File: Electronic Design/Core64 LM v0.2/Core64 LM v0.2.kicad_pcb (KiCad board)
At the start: 2 copper layers, 85 x 85 mm, 88 parts, among them J1 PASS THROUGH BOARD, J2 PASS THROUGH BOARD, J3 Conn_01x01_Male, J4 Conn_01x01_Male, J5 Conn_01x01_Male, J6 Conn_01x01_Male

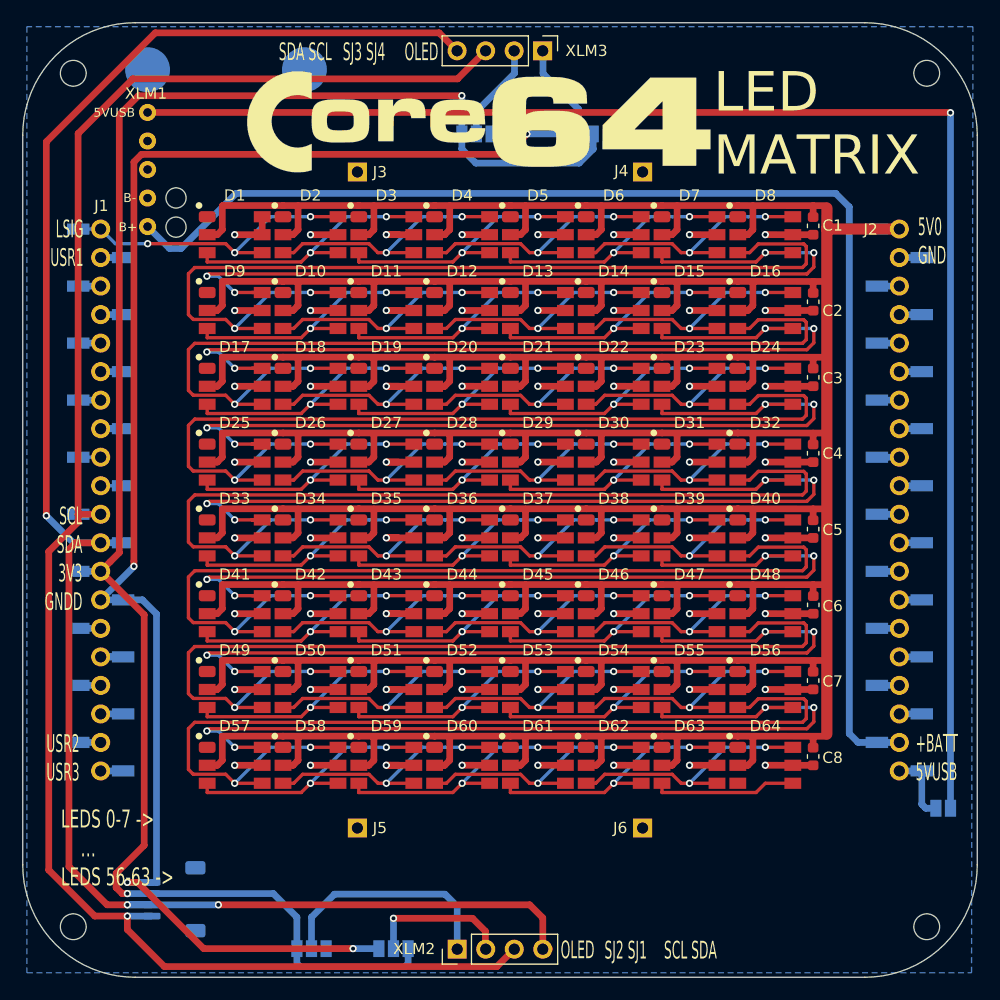
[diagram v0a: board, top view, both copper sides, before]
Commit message: Refine layout placement of QWIIC and silkscreen, add battery markers
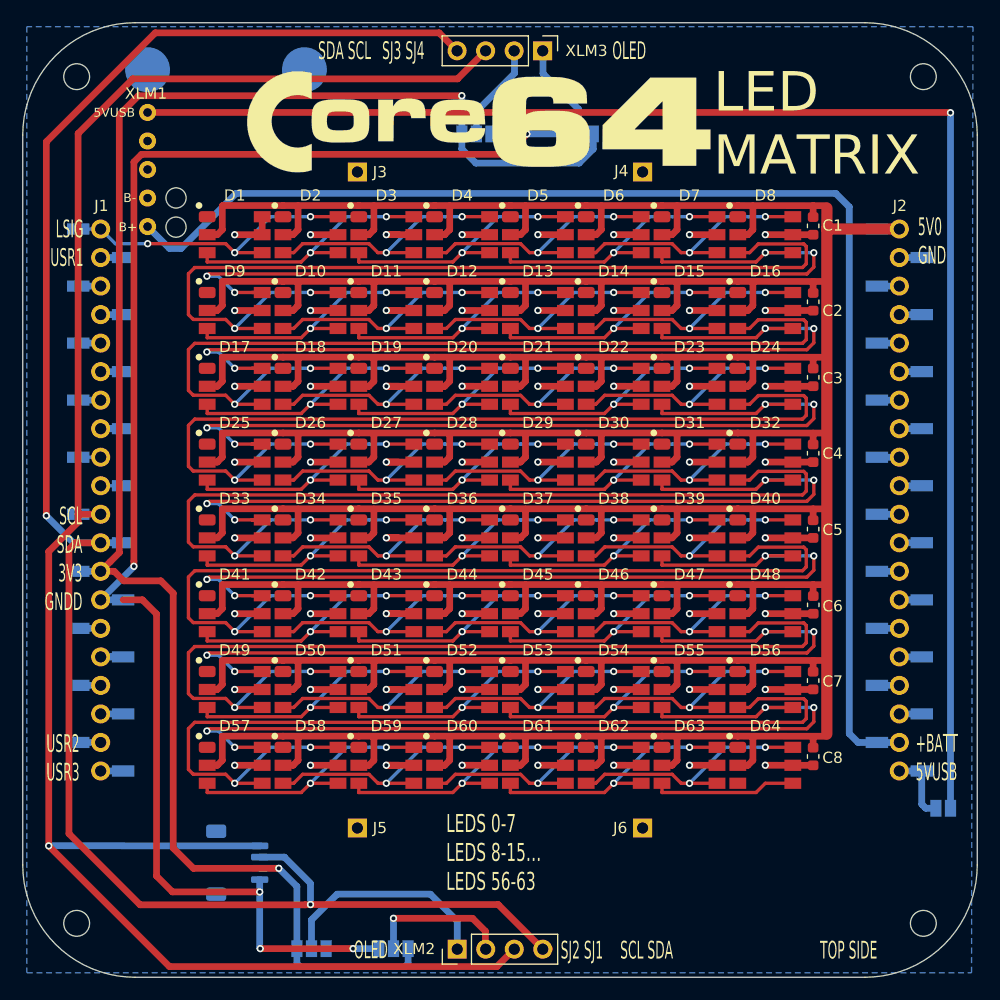
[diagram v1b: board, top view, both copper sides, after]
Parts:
- moved XLM4 6.47 mm to (-23.4, 32.3), turned to 90 degrees
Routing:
- net I2C_CLOCK: track 158.2 -> 173.0 mm
- net GNDD: track 143.9 -> 140.2 mm, vias 4 -> 5
- net I2C_DATA: track 163.1 -> 164.9 mm, vias 3 -> 2
- net 3V3: track 156.7 -> 155.6 mm
- net Net-(JP2-Pad2): track 20.9 -> 20.0 mm
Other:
- outline, holes or cut-outs redrawn
- board text added: "<-Battery Corner"
- board text added: "BOTTOM SIDE"
- board text added: "CORE64 LED MATRIX (LM) V0.2 2021-03-13 Project information at www.Core64.io Designed by Andy Geppert at www.MachineIdeas.com WS2813 LEDs"
- board text added: "JLCJLCJLCJLC"
- board text added: "LEDS 0-7 LEDS 8-15… LEDS 56-63"
- board text added: "TOP SIDE"
- board text removed: "+B"
- board text removed: "-B"
- board text removed: "CORE64 LED MATRIX (LM) V0.2 2021-03-08"
- board text removed: "GNDD 3V3 SDA SCL"
- board text removed: "LEDS 0-7 -> … LEDS 56-63 ->"
- board text removed: "Project information at www.Core64.io Designed by Andy Geppert at www.MachineIdeas.com WS2813 LEDs"

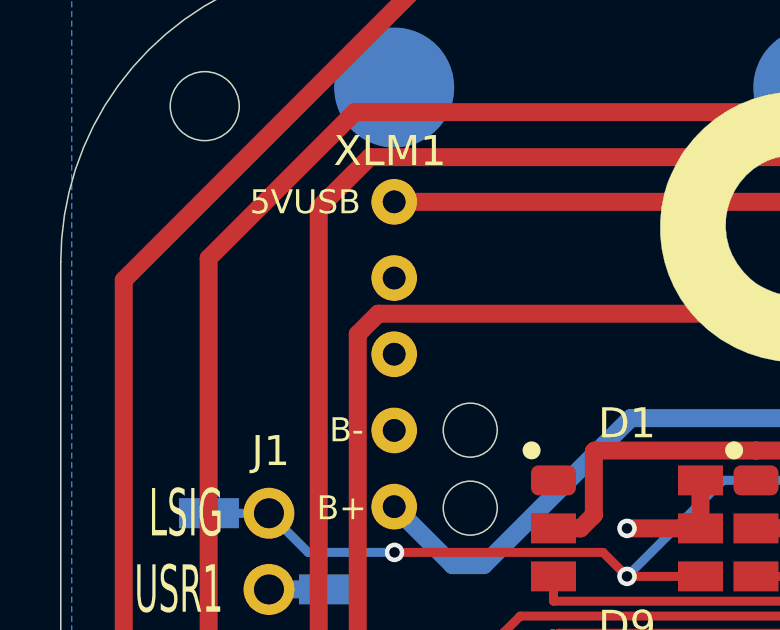
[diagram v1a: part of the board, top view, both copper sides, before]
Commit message: Tweak LiPo charger silkscreen
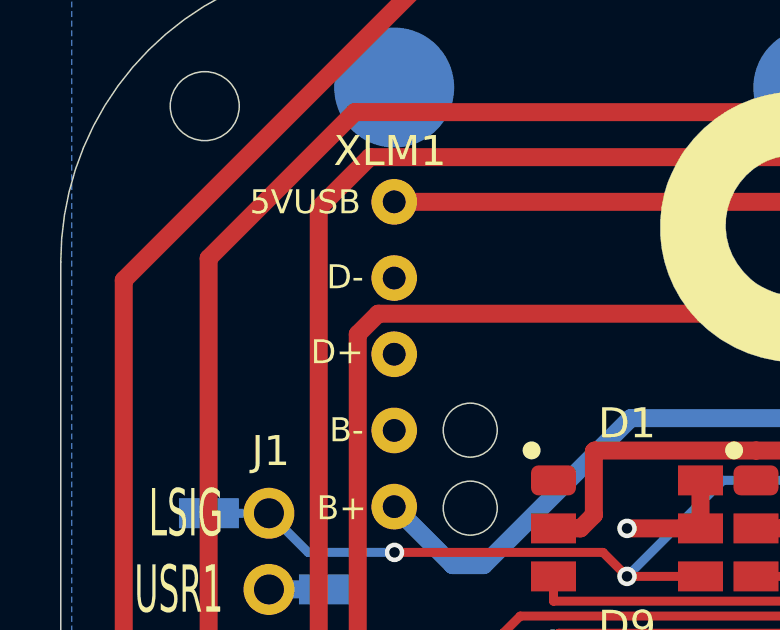
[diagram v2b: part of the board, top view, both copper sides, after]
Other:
- board text added: "D+"
- board text added: "D-"
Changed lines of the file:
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@@
   (general
     (thickness 1.6)
-    (drawings 105)
+    (drawings 107)
     (tracks 1399)
     (zones 0)
@@
     )
   )
+  (gr_text D- (at -32.4 -32) (layer F.SilkS)
+    (effects (font (size 0.8 0.8) (thickness 0.16)) (justify right))
+  )
+  (gr_text D+ (at -32.4 -29.5) (layer F.SilkS)
+    (effects (font (size 0.8 0.8) (thickness 0.16)) (justify right))
+  )
   (gr_line (start -16 -25) (end -16 -27) (layer B.SilkS) (width 0.16))

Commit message: Add "Teensy Charge Enable" to silkscreen
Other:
- board text added: "TEENSY CHARGE ENABLE"
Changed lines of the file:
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@@
   (general
     (thickness 1.6)
-    (drawings 107)
+    (drawings 108)
     (tracks 1399)
     (zones 0)
@@
     (tags "solder jumper open")
     (attr virtual)
-    (fp_text reference JP5 (at -0.15 -2.1) (layer B.SilkS)
+    (fp_text reference JP5 (at 2.865 0.05) (layer B.SilkS)
       (effects (font (size 1 1) (thickness 0.15)) (justify mirror))
     )
@@
     )
   )
+  (gr_text "TEENSY\nCHARGE\nENABLE" (at 42.3 31.1) (layer B.SilkS)
+    (effects (font (size 1 1) (thickness 0.15)) (justify left mirror))
+  )
   (gr_text D- (at -32.4 -32) (layer F.SilkS)

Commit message: Release LM V0.2 Gerbers and assembly files
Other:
- board text added: "CORE64 LED MATRIX (LM) V0.2 2021-03-21 Project information at www.Core64.io Designed by Andy Geppert at www.MachineIdeas.com WS2813 LEDs"
- board text removed: "CORE64 LED MATRIX (LM) V0.2 2021-03-13 Project information at www.Core64.io Designed by Andy Geppert at www.MachineIdeas.com WS2813 LEDs"
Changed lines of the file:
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@@
       (drillshape 0)
       (scaleselection 1)
-      (outputdirectory "Core64_LM_V0.1_Gerbers/"))
+      (outputdirectory "Core64_LM_V0.2_Gerbers/"))
   )
   (net 0 "")
@@
     (arrow2b (pts (xy 42.5 -50.549999) (xy 41.373496 -49.963578)))
   )
-  (gr_text "CORE64 LED MATRIX (LM)     V0.2     2021-03-13\nProject information at www.Core64.io\nDesigned by Andy Geppert at www.MachineIdeas.com\nWS2813 LEDs" (at 35.7 34.5) (layer B.SilkS)
+  (gr_text "CORE64 LED MATRIX (LM)     V0.2     2021-03-21\nProject information at www.Core64.io\nDesigned by Andy Geppert at www.MachineIdeas.com\nWS2813 LEDs" (at 35.7 34.5) (layer B.SilkS)
     (effects (font (size 1.2 1.2) (thickness 0.15)) (justify left mirror))
   )

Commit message: Correct mistake, extend trace to pad 14 on J1 from bottom GNND of QWIIC and XLM2
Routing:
- net GNDD: track 140.2 -> 142.2 mm
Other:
- board text added: "Battery Limits: 1S or 3.3-7.5V"
- board text removed: "Battery Limits: 1s or 3.3-7.5V"
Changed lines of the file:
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@@
     (effects (font (size 1 1) (thickness 0.15)) (justify left mirror))
   )
-  (gr_text "Battery Limits:\n1s or 3.3-7.5V" (at 34.25 -33.25) (layer B.SilkS)
+  (gr_text "Battery Limits:\n1S or 3.3-7.5V" (at 34.25 -33.25) (layer B.SilkS)
     (effects (font (size 1.5 1.5) (thickness 0.3)) (justify left mirror))
   )
@@
   (via (at -21.4 34.9) (size 0.65) (drill 0.35) (layers F.Cu B.Cu) (net 166))
   (segment (start -21.4 34.9) (end -21.4 39.9) (width 0.6) (layer B.Cu) (net 166))
+  (segment (start -21.4 33.8) (end -21.4 34.9) (width 0.6) (layer B.Cu) (net 166))
   (segment (start -29.17 34.9) (end -21.4 34.9) (width 0.6) (layer F.Cu) (net 166))
   (segment (start -30.585 33.485) (end -29.17 34.9) (width 0.6) (layer F.Cu) (net 166))
   (segment (start -30.585 10.15) (end -30.585 33.485) (width 0.6) (layer F.Cu) (net 166))
   (segment (start -31.845 8.89) (end -30.585 10.15) (width 0.6) (layer F.Cu) (net 166))
-  (segment (start -33.56 8.89) (end -31.845 8.89) (width 0.6) (layer F.Cu) (net 166))
-  (segment (start -21.4 33.8) (end -21.4 34.9) (width 0.6) (layer B.Cu) (net 166))
+  (segment (start -35.56 8.89) (end -31.845 8.89) (width 0.6) (layer F.Cu) (net 166))
   (via (at -9.485 37.25) (size 0.65) (drill 0.35) (layers F.Cu B.Cu) (net 167))
   (segment (start -9.485 39.95) (end -9.485 37.25) (width 0.6) (layer B.Cu) (net 167))
